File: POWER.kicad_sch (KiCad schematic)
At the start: 17 parts, among them U2 AMS1117-3.3, U3 LM2576HVS-ADJ

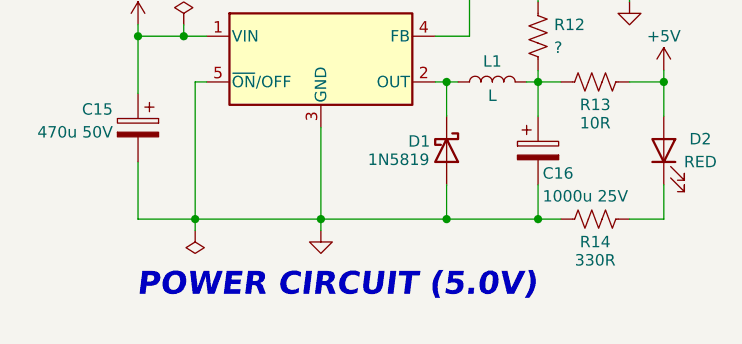
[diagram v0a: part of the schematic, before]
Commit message: Specefies which section is complete and incomplete
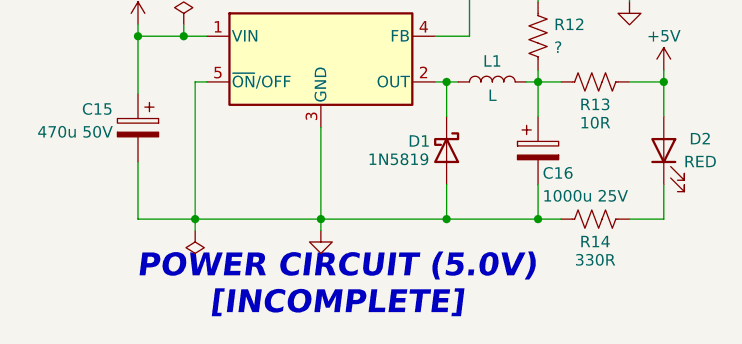
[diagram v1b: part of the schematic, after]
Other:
- note added: "POWER CIRCUIT (5.0V) [INCOMPLETE]"
- note removed: "POWER CIRCUIT (5.0V)"
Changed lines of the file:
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@@
 	(generator_version "10.0")
 	(paper "A4")
-	(text "POWER CIRCUIT (5.0V)"
+	(text "POWER CIRCUIT (5.0V)\n[INCOMPLETE]"
 		(exclude_from_sim no)
 		(at 84.328 88.646 0)

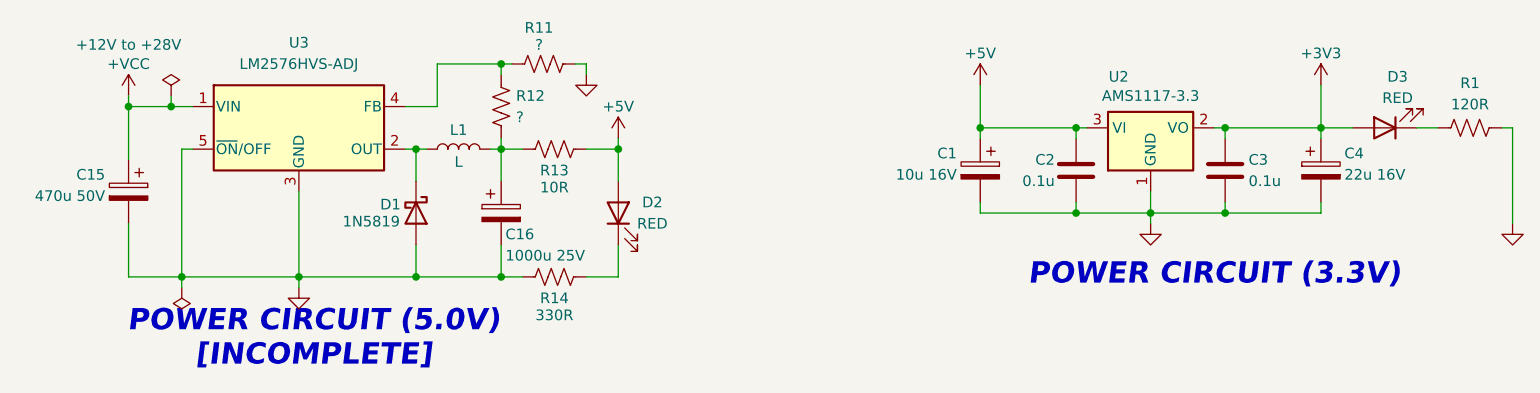
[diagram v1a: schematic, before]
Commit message: Optocoupler added for RS485 communication (DEBUG_and_COM)
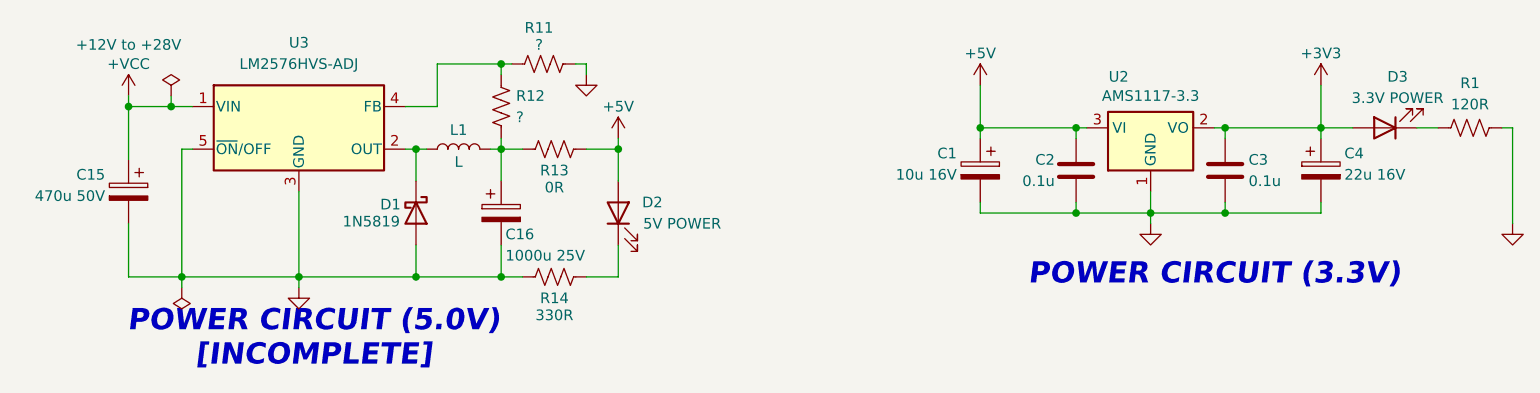
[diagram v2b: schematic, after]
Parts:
- D2: value RED -> 5V POWER; Information (none) -> 5V Power indicator (Red)
- D3: value RED -> 3.3V POWER; Information (none) -> 3.3V Power indicator (RED)
- R13: value 10R -> 0R
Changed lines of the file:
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@@
 			)
 		)
-		(property "Value" "10R"
+		(property "Value" "0R"
 			(at 113.03 70.612 90)
 			(show_name no)
@@
 			)
 		)
-		(property "Value" "RED"
+		(property "Value" "3.3V POWER"
 			(at 213.614 59.944 0)
 			(show_name no)
@@
 		)
 		(property "Sim.Pins" "1=K 2=A"
+			(at 212.09 63.5 0)
+			(hide yes)
+			(show_name no)
+			(do_not_autoplace no)
+			(effects
+				(font
+					(size 1.27 1.27)
+				)
+			)
+		)
+		(property "Information" "3.3V Power indicator (RED)"
 			(at 212.09 63.5 0)
 			(hide yes)
@@
 			)
 		)
-		(property "Value" "RED"
-			(at 124.714 74.93 90)
+		(property "Value" "5V POWER"
+			(at 128.27 74.93 90)
 			(show_name no)
 			(do_not_autoplace no)
@@
 			(hide yes)
 			(show_name no)
+			(do_not_autoplace no)
+			(effects
+				(font
+					(size 1.27 1.27)
+				)
+			)
+		)
+		(property "Information" "5V Power indicator (Red)"
+			(at 120.65 73.66 90)
+			(hide yes)
+			(show_name no)
